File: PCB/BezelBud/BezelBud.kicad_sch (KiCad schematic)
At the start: 31 parts, among them J1 USB_C_Receptacle_USB2.0_14P, U1 USBLC6-2SC6, U2 STM32F103C8T6, U3 XC6206P332MR, U4 XC6206P332MR, U5 E7243E

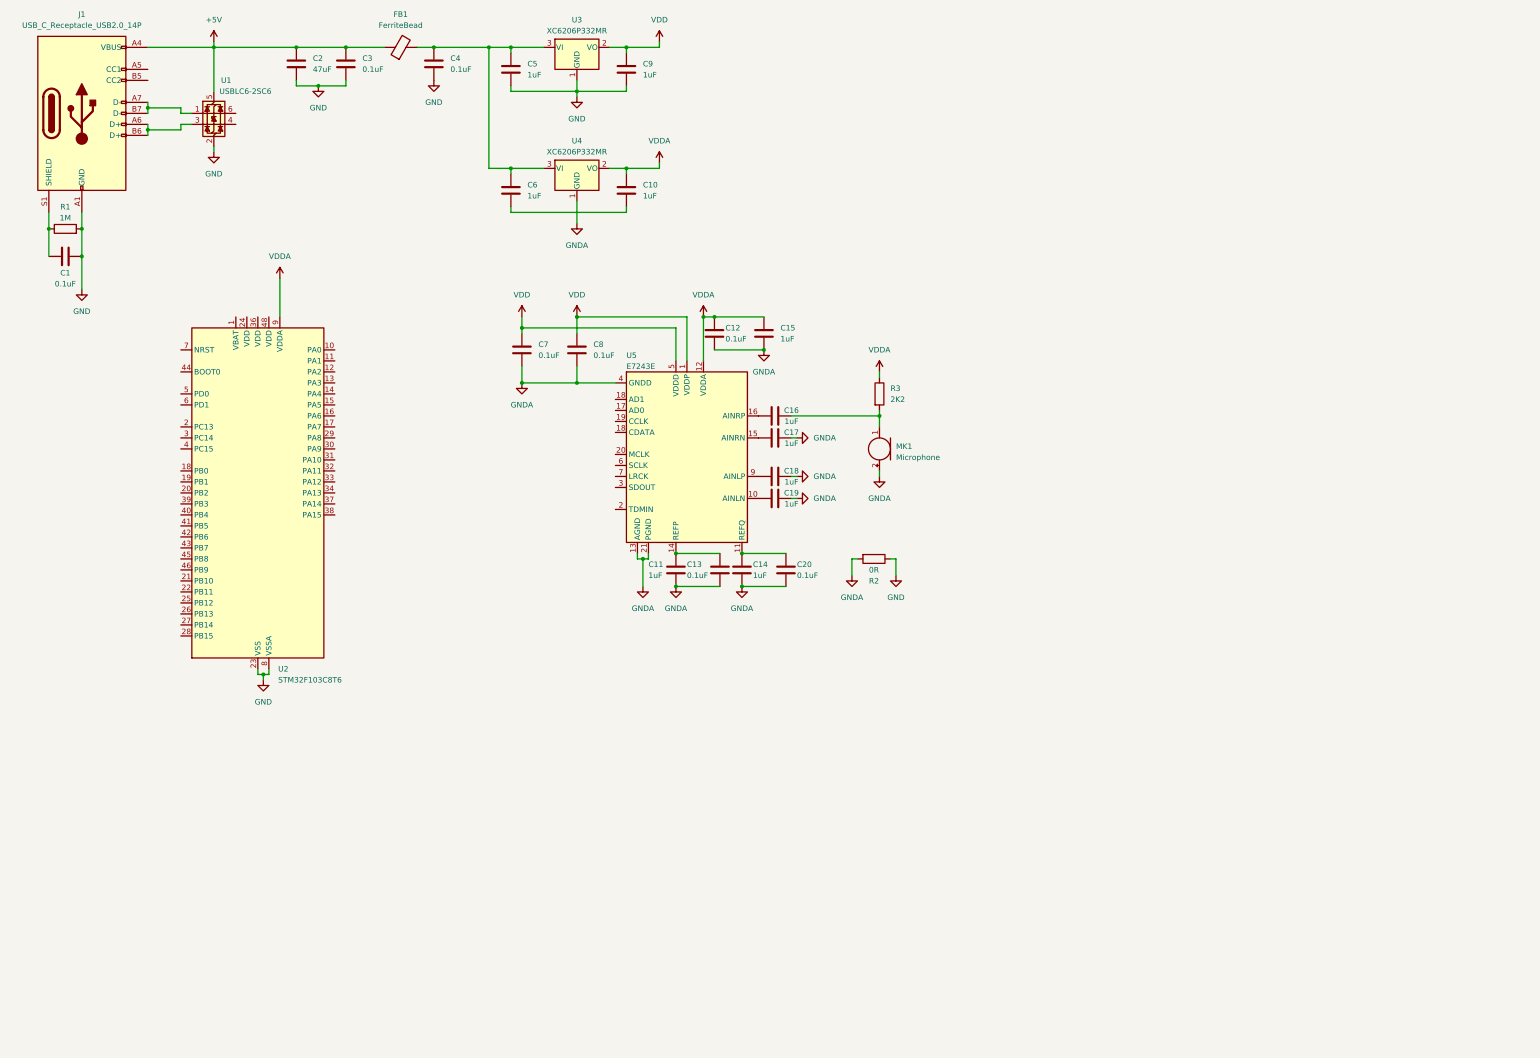
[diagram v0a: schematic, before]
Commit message: Added parts to schematic
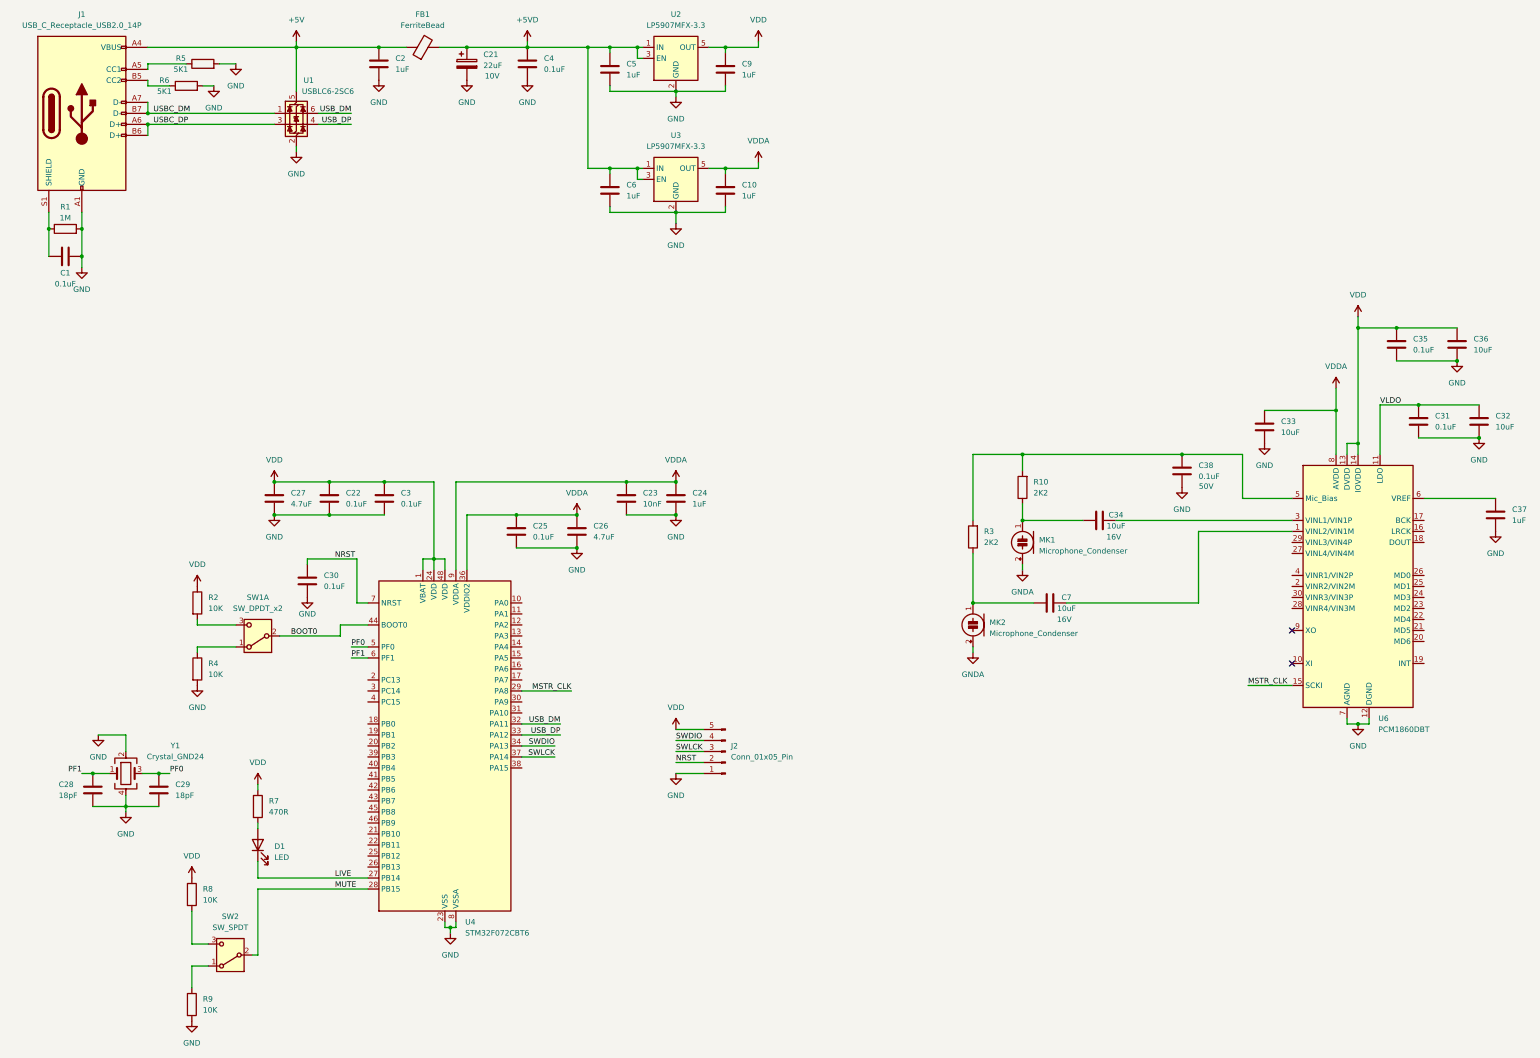
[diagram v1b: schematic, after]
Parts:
- removed C11, C14, C15, C16, C17, C18, C19: 1uF, Capacitor_SMD:C_0603_1608Metric, symbol Device:C
- removed C12, C13, C20, C8: 0.1uF, Capacitor_SMD:C_0603_1608Metric, symbol Device:C
- removed MK1: Microphone, symbol Device:Microphone
- removed U2: STM32F103C8T6, Package_QFP:LQFP-48_7x7mm_P0.5mm, symbol MCU_ST_STM32F1:STM32F103C8Tx
- removed U3, U4: XC6206P332MR, Package_TO_SOT_SMD:SOT-23-3, symbol Regulator_Linear:XC6206PxxxMR
- removed U5: E7243E, symbol BezelBud:ES7243E
- added C21: 22uF, Capacitor_Tantalum_SMD:CP_EIA-3216-10_Kemet-I, symbol Device:C_Polarized
- added C22, C25, C30, C31, C35, C38: 0.1uF, Capacitor_SMD:C_0603_1608Metric, symbol Device:C
- added C23: 10nF, Capacitor_SMD:C_0603_1608Metric, symbol Device:C
- added C24, C37: 1uF, Capacitor_SMD:C_0603_1608Metric, symbol Device:C
- added C26, C27: 4.7uF, Capacitor_SMD:C_0603_1608Metric, symbol Device:C
- added C28, C29: 18pF, Capacitor_SMD:C_0603_1608Metric, symbol Device:C
- added C32, C33, C34, C36: 10uF, Capacitor_SMD:C_0603_1608Metric, symbol Device:C
- added D1: LED, symbol Device:LED
- added J2: Conn_01x05_Pin, symbol Connector:Conn_01x05_Pin
- added MK1, MK2: Microphone_Condenser, symbol Device:Microphone_Condenser
- added R10: 2K2, Resistor_SMD:R_0603_1608Metric, symbol Device:R
- added R4, R8, R9: 10K, Resistor_SMD:R_0603_1608Metric, symbol Device:R
- added R5, R6: 5K1, Resistor_SMD:R_0603_1608Metric, symbol Device:R
- added R7: 470R, Resistor_SMD:R_0603_1608Metric, symbol Device:R
- added SW1: SW_DPDT_x2, Connector_PinHeader_2.54mm:PinHeader_1x03_P2.54mm_Vertical, symbol Switch:SW_DPDT_x2
- added SW2: SW_SPDT, symbol Switch:SW_SPDT
- added U2, U3: LP5907MFX-3.3, Package_TO_SOT_SMD:SOT-23-5, symbol Regulator_Linear:LP5907MFX-3.3
- added U4: STM32F072CBT6, Package_QFP:LQFP-48_7x7mm_P0.5mm, symbol MCU_ST_STM32F0:STM32F072CBTx
- added U6: PCM1860DBT, Package_SO:TSSOP-30_4.4x7.8mm_P0.5mm, symbol Audio:PCM1860DBT
- added Y1: Crystal_GND24, symbol Device:Crystal_GND24
- C2: value 47uF -> 1uF; footprint Capacitor_SMD:C_1210_3225Metric -> Capacitor_SMD:C_0603_1608Metric; Supplier https://www.lcsc.com/product-detail/C5440143.html?s_z=n_47uf -> (none)
- C7: value 0.1uF -> 10uF; Rating (none) -> 16V
- R2: value 0R -> 10K
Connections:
- net +5V: no longer C3.1
- net GND: now also C10.2, C6.2, C21.2, C22.2, C23.2, C24.2, C25.2, C26.2, C27.2, C28.2, C29.2, C30.2, C31.2, C32.2, C33.2, C35.2, C36.2, C37.2, C38.2, J2.1 (Pin_1), R4.2, R5.2, R6.2, R9.2, U2.2 (GND), U3.2 (GND), U4.23 (VSS), U4.35 (VSS), U4.47 (VSS), U4.8 (VSSA), U6.12 (DGND), U6.7 (AGND), Y1.2, Y1.4; no longer R2.1
- net GNDA: now also MK1.2 (+), MK2.2 (+); no longer C7.2, R2.2
- net VDD: now also C3.1, R2.1, C22.1, C27.1, C35.1, C36.1, J2.5 (Pin_5), R7.1, R8.1, U2.5 (OUT), U4.1 (VBAT), U4.24 (VDD), U4.48 (VDD), U6.13 (DVDD), U6.14 (IOVDD); no longer C7.1
- net VDDA: now also C23.1, C24.1, C25.1, C26.1, C33.1, U3.5 (OUT), U4.36 (VDDIO2), U4.9 (VDDA), U6.8 (AVDD); no longer R3.1
- net +5VD: now reaches C4.1, C5.1, C6.1, FB1.2
- net +5VD: now also C21.1, U2.1 (IN), U2.3 (EN), U3.1 (IN), U3.3 (EN)
- net at J1.A5 (CC1): now also R5.1
- net USBC_DP: now reaches J1.A6 (D+), J1.B6 (D+), U1.3 (I/O2)
- net USBC_DM: now reaches J1.A7 (D-), J1.B7 (D-), U1.1 (I/O1)
- net at J1.B5 (CC2): now also R6.1
- net at R3.2: now also C38.1, R10.2, U6.5 (Mic_Bias)
- net USB_DP: now reaches U1.4 (I/O2)
- net USB_DP: now also U4.33 (PA12)
- net USB_DM: now reaches U1.6 (I/O1)
- net USB_DM: now also U4.32 (PA11)
- new net: C34.1, MK1.1 (-), R10.1
- new net: C7.1, MK2.1 (-), R3.1
- new net: C7.2, U6.1 (VINL2/VIN1M)
- new net: C37.1, U6.6 (VREF)
- new net: C34.2, U6.3 (VINL1/VIN1P)
- new net: R9.1, SW2.1 (A)
- new net: R8.2, SW2.3 (C)
- new net: D1.2 (A), R7.2
- new net: R4.1, SW1.1 (A)
- new net: R2.2, SW1.3 (C)
- new net BOOT0: SW1.2 (B), U4.44 (BOOT0)
- new net LIVE: D1.1 (K), U4.27 (PB14)
- new net MSTR_CLK: U4.29 (PA8), U6.15 (SCKI)
- new net MUTE: SW2.2 (B), U4.28 (PB15)
- new net NRST: C30.1, J2.2 (Pin_2), U4.7 (NRST)
- new net PF0: C29.1, U4.5 (PF0), Y1.3
- new net PF1: C28.1, U4.6 (PF1), Y1.1
- new net SWDIO: J2.4 (Pin_4), U4.34 (PA13)
- new net SWLCK: J2.3 (Pin_3), U4.37 (PA14)
- new net VLDO: C31.1, C32.1, U6.11 (LDO)
- no-connect marks 0 -> 2
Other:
- moved on the sheet: C10, C4, C5, C6, C9, FB1, U1

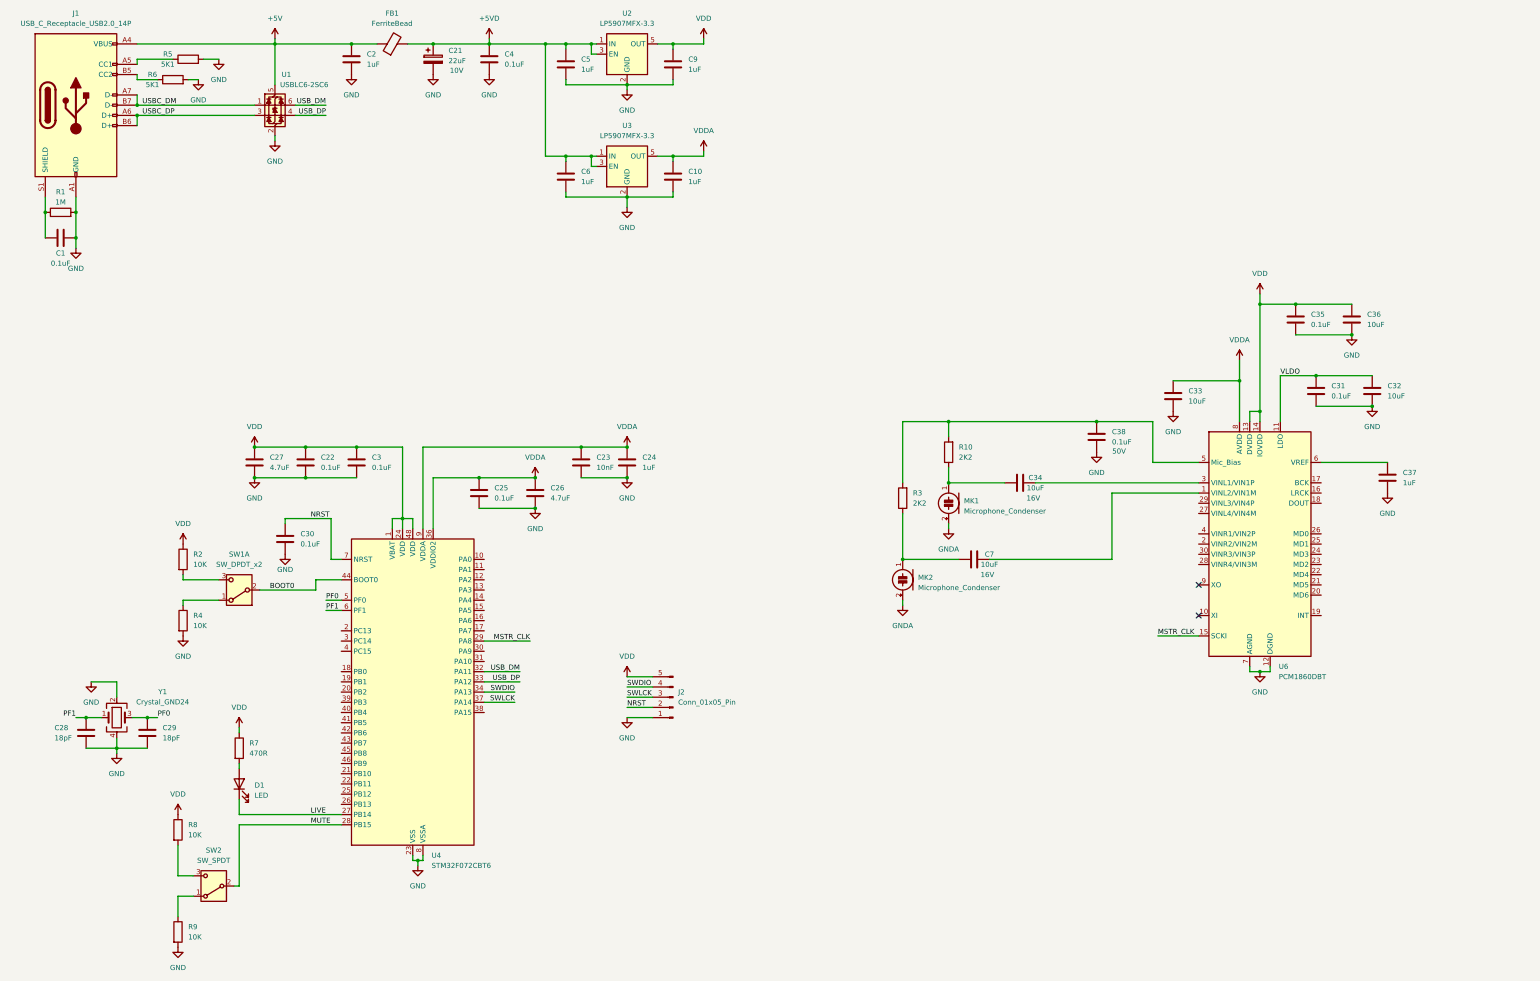
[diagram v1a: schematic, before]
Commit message: updated firmware and schematic
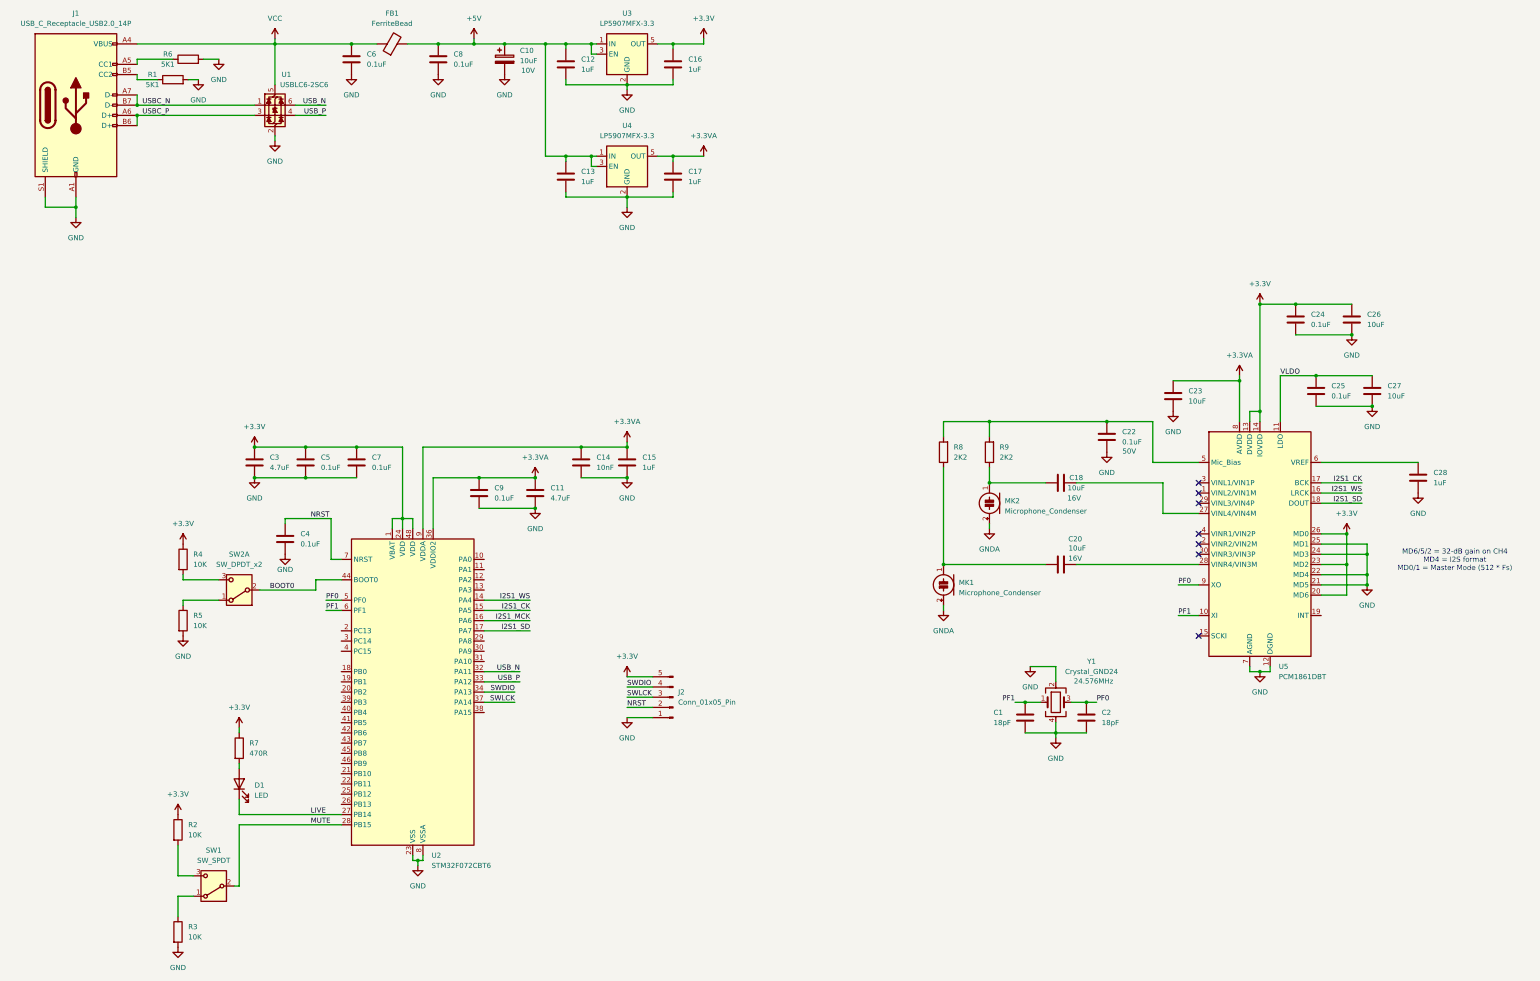
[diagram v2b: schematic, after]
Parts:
- removed C1: 0.1uF, Capacitor_SMD:C_0603_1608Metric, symbol Device:C
- removed R1: 1M, Resistor_SMD:R_0603_1608Metric, symbol Device:R
- C10: renamed from C21; value 22uF -> 10uF; footprint Capacitor_Tantalum_SMD:CP_EIA-3216-10_Kemet-I -> Capacitor_Tantalum_SMD:CP_EIA-3216-18_Kemet-A
- C6: renamed from C2; value 1uF -> 0.1uF
- U5: renamed from U6; value PCM1860DBT -> PCM1861DBT
- Y1: footprint (none) -> Crystal:Crystal_SMD_3225-4Pin_3.2x2.5mm; Freq (none) -> 24.576MHz; Supplier  (none) -> https://www.lcsc.com/product-detail/C41383247.html
- renumbered C28 to C1, C26 to C11, C5 to C12, C6 to C13, C23 to C14, C24 to C15, C9 to C16, C10 to C17, C34 to C18, C29 to C2, C7 to C20, C38 to C22, C33 to C23, C35 to C24, C31 to C25, C36 to C26, C32 to C27, C37 to C28, C27 to C3, C30 to C4, C22 to C5, C3 to C7, C4 to C8, C25 to C9, MK2 to MK1, MK1 to MK2, R6 to R1, R8 to R2, R9 to R3, R2 to R4, R4 to R5, R5 to R6, R3 to R8, R10 to R9, SW2 to SW1, SW1 to SW2, U4 to U2, U2 to U3, U3 to U4
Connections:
- net +5VD is gone; now on net +5V: C10.1, C12.1, C13.1, C8.1, FB1.2, U3.1 (IN), U3.3 (EN), U4.1 (IN), U4.3 (EN)
- net VDD is gone; now on net +3.3V: C16.1, C24.1, C26.1, C3.1, C5.1, C7.1, J2.5 (Pin_5), R2.1, R4.1, R7.1, U2.1 (VBAT), U2.24 (VDD), U2.48 (VDD), U3.5 (OUT), U5.13 (DVDD), U5.14 (IOVDD)
- net +5V: no longer C6.1, FB1.1, J1.A4 (VBUS), J1.A9 (VBUS), J1.B4 (VBUS), J1.B9 (VBUS), U1.5 (VBUS)
- net GND: now also J1.S1 (SHIELD), U5.21 (MD5), U5.22 (MD4), U5.24 (MD3), U5.25 (MD1)
- net PF0: now also U5.9 (XO)
- net PF1: now also U5.10 (XI)
- net at C20.2: now also U5.28 (VINR4/VIN3M); no longer U5.1 (VINL2/VIN1M)
- net I2S1_WS: now reaches U5.16 (LRCK)
- net I2S1_WS: now also U2.14 (PA4)
- net I2S1_CK: now reaches U5.17 (BCK)
- net I2S1_CK: now also U2.15 (PA5)
- net I2S1_SD: now reaches U5.18 (DOUT)
- net I2S1_SD: now also U2.17 (PA7)
- net +3.3V: now reaches U5.20 (MD6)
- net +3.3V: now also U5.23 (MD2), U5.26 (MD0)
- net at U5.27 (VINL4/VIN4M): now also C18.2
- net at U5.3 (VINL1/VIN1P): no longer C18.2
- net I2S1_MCK: now reaches U2.16 (PA6)
- net MSTR_CLK: no longer names the net of U5.15 (SCKI)
- net MSTR_CLK: no longer U2.29 (PA8)
- net USBC_DM renamed USBC_N
- net USBC_DP renamed USBC_P
- net USB_DM renamed USB_N
- net USB_DP renamed USB_P
- net VDDA renamed +3.3VA
- new net VCC: C6.1, FB1.1, J1.A4 (VBUS), J1.A9 (VBUS), J1.B4 (VBUS), J1.B9 (VBUS), U1.5 (VBUS)
- no-connect marks 2 -> 7
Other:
- note added: "MD6/5/2 = 32-dB gain on CH4 MD4 = I2S format MD0/1 = Master Mode (512 * Fs)"
- moved on the sheet: C1, C10, C18, C2, C20, C22, C28, C8, MK1, MK2, R8, R9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
